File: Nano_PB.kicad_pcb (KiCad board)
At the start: 2 copper layers, 100 x 40 mm, 97 parts, among them CON1 BARREL_JACK, P1 CONN_01X06, P2 CONN_01X01, P3 CONN_01X03, P4 CONN_01X03, P5 CONN_01X03, P6 CONN_01X04, Q1 SMBT3904, Q10 BSS138, Q2 SMBT3904, Q3 SMBT3904, Q4 SMBT3904, Q5 SMBT3904, Q6 BC846B, Q7 BC846B, Q8 BC846B, Q9 BSS138, SW1 Izquierda, SW2 Arriba, SW3 Abajo, SW4 Derecha, U1 Arduino_Nano, U2 LM7805CT, U3 Matriz_5x7, U4 74HC595, U5 74HC595, U6 74HC148, U7 MMA7660FC

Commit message: corrige issue #10
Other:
- board text added: "ClkIn-D13"
- board text added: "Din-D12"
- board text removed: "ClkIn-D12"
- board text removed: "Din-D13"
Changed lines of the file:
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@@
-(kicad_pcb (version 4) (host pcbnew 4.1.0-alpha+201608060946+7009~46~ubuntu14.04.1-product)
+(kicad_pcb (version 20160815) (host pcbnew 4.1.0-alpha+201608271546+7097~46~ubuntu14.04.1-product)
   (general
     (links 193)
@@
     (uvia_dia 0.3)
     (uvia_drill 0.1)
+    (diff_pair_gap 0.25)
+    (diff_pair_width 0.2)
     (add_net +3V3)
     (add_net A0)
@@
     (uvia_dia 0.3)
     (uvia_drill 0.1)
+    (diff_pair_gap 0.25)
+    (diff_pair_width 0.2)
     (add_net +5V)
     (add_net "Net-(CON1-Pad1)")
@@
     (effects (font (size 1 1) (thickness 0.15)) (justify mirror))
   )
-  (gr_text ClkIn-D12 (at 84.26 70.24) (layer B.SilkS)
+  (gr_text ClkIn-D13 (at 84.26 70.24) (layer B.SilkS)
     (effects (font (size 1 1) (thickness 0.15)) (justify mirror))
   )
-  (gr_text Din-D13 (at 84.97 68.19) (layer B.SilkS)
+  (gr_text Din-D12 (at 84.97 68.19) (layer B.SilkS)
     (effects (font (size 1 1) (thickness 0.15)) (justify mirror))
   )

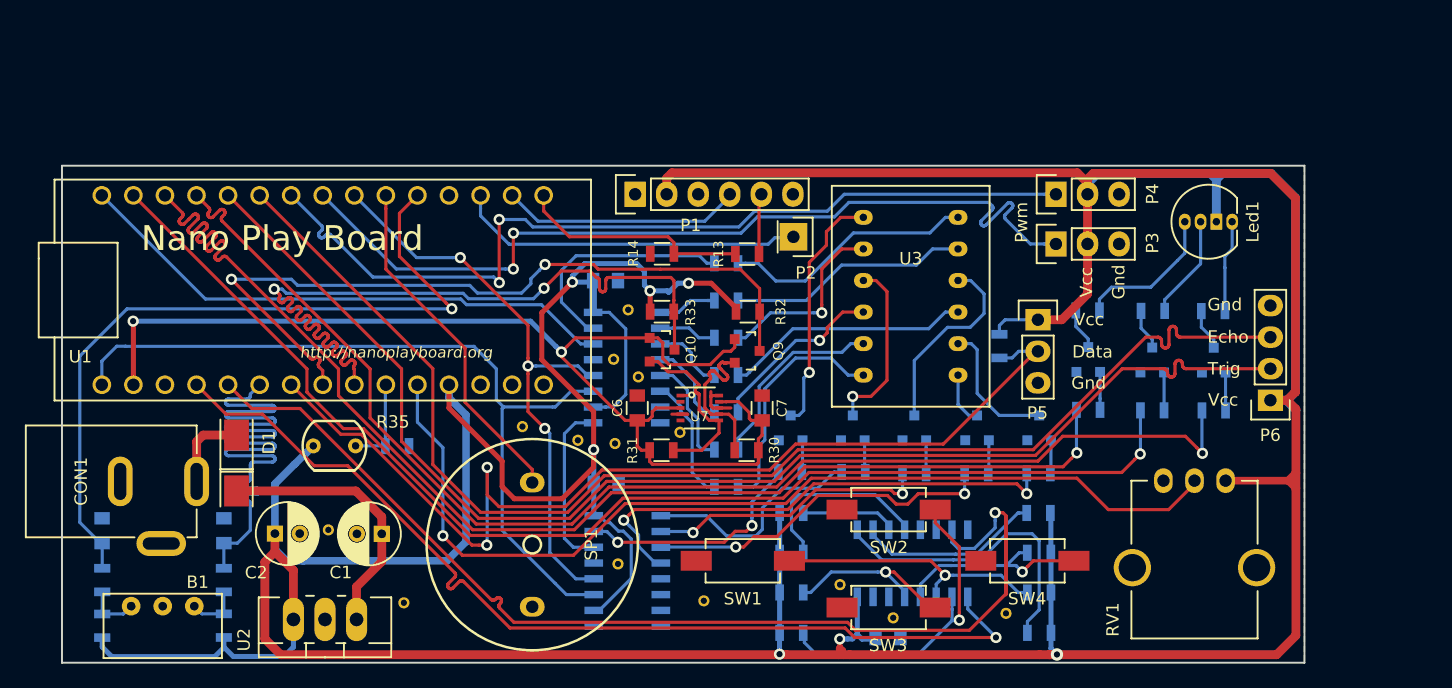
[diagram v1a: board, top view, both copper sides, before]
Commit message: cambiados encoder y potenciometro
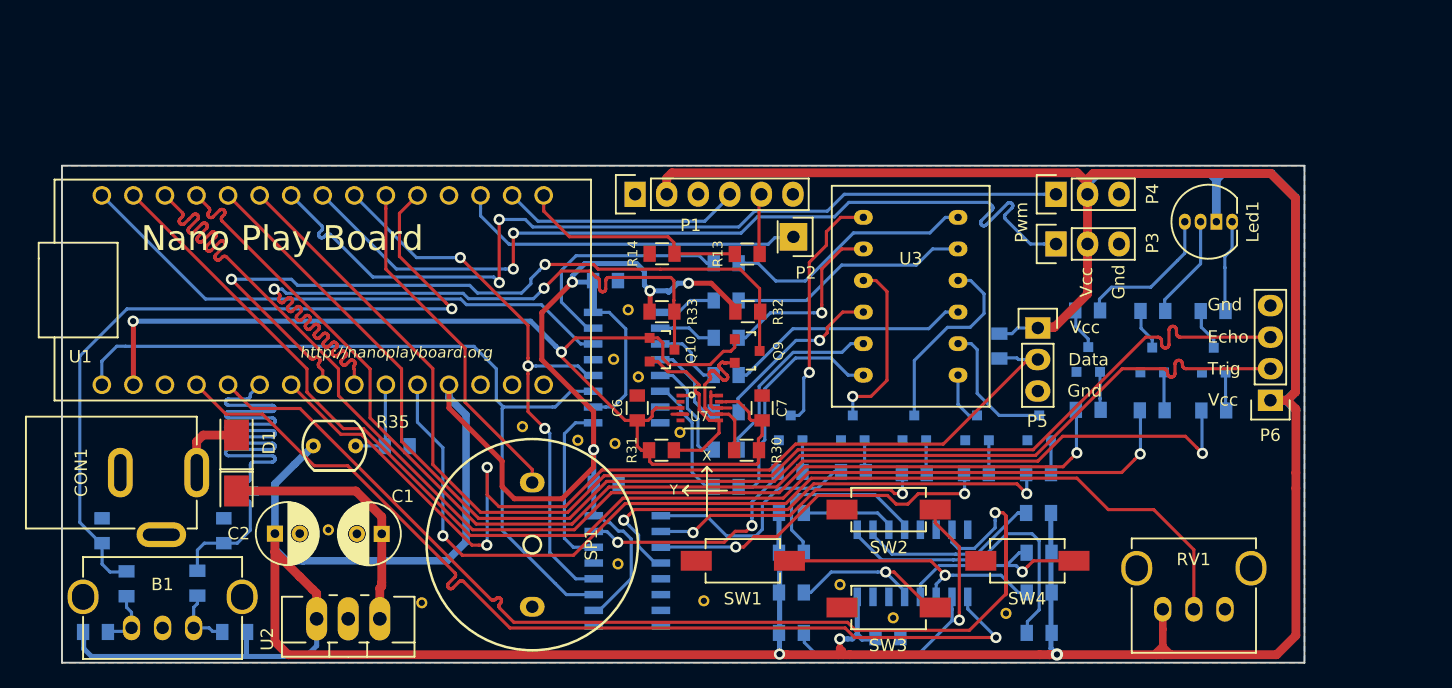
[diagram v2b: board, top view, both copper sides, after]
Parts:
- B1: footprint Sensores:Bourns_3315C_encoder_incremental -> Sensores:ALPS_EC12E24_encoder_incremental
- R1, R10, R11, R12, R13, R14, R15, R16, R17, R18, R19, R2, R20, R21, R22, R23, R24, R25, R26, R27, R28, R29, R3, R30, R31, R32, R33, R36, R37, R38, R39, R4, R40, R5, R6, R7, R8, R9: footprint Resistors_SMD:R_0805 -> Resistencias:R_0805
- RV1: footprint Potenciometros:POT_SR_PASIVES_R9011 -> Potenciometros:ALP_RK09K111
- moved RV1 10.4 mm to (143.2, 70.5), turned to 0 degrees
- moved R40 2.14 mm to (63.0, 68.4)
- moved R38 1.98 mm to (57.3, 68.4)
- moved U2 1.87 mm to (75.1, 71.2)
- moved B1 1.75 mm to (60.2, 72.0), turned to 0 degrees
- moved Gnd-Via 1.44 mm to (81.0, 70.0)
- moved R39 1.01 mm to (66.0, 72.3), turned to 180 degrees
- moved R37 0.74 mm to (54.8, 72.3), turned to 0 degrees
- moved CON1 0.71 mm to (62.9, 59.5)
- moved P5 0.66 mm to (130.6, 47.8)
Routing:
- net A7: track 78.9 -> 83.8 mm
- net +5V: track 477.2 -> 479.9 mm
- net A2: track 61.0 -> 63.1 mm
- net D2: track 60.9 -> 62.8 mm
- net Net-(C1-Pad1): track 21.6 -> 20.8 mm
- net Net-(B1-PadB): track 4.41 -> 5.19 mm
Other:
- board text added: "10/16"
- board text added: "Rev-0.2.1"
- board text added: "X"
- board text added: "Y"
- board text removed: "08/16"
- board text removed: "Rev-0.2"

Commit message: añadidos driver para led y conectores para fotodiodos infrarrojos
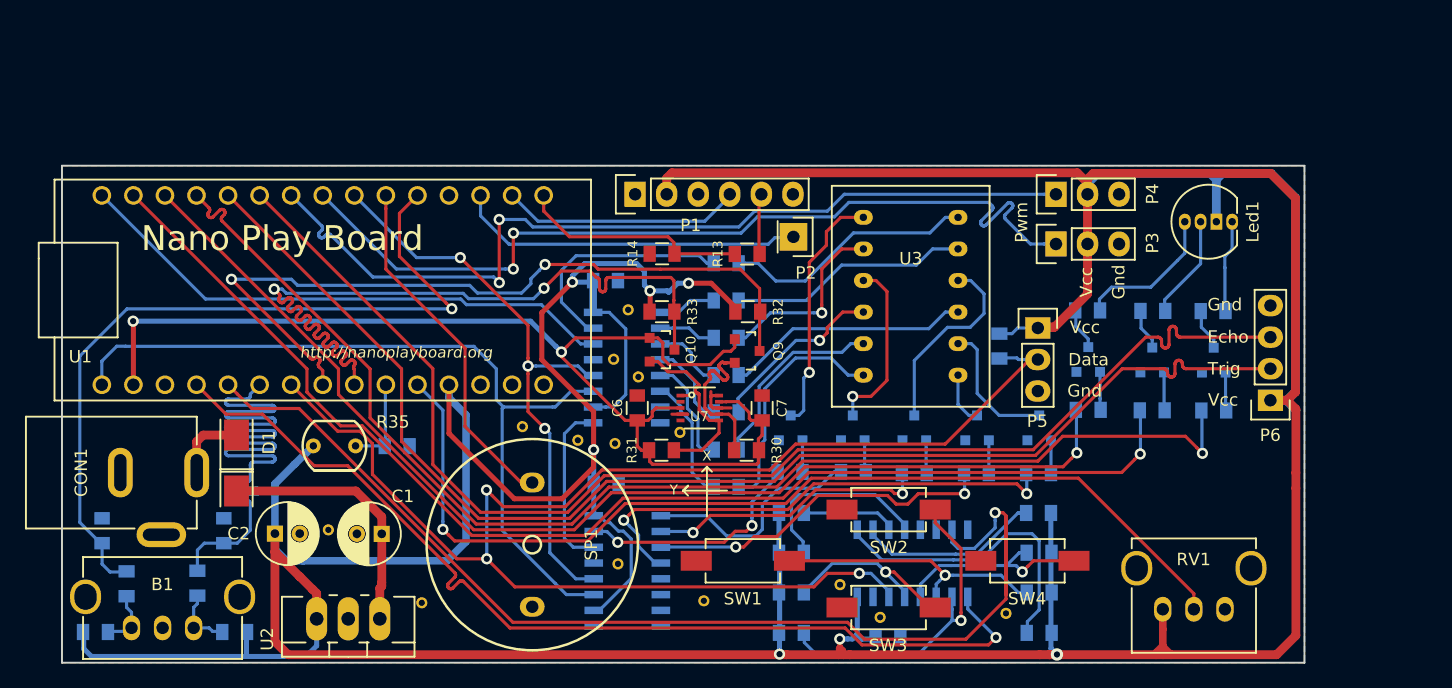
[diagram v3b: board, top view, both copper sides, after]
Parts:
- moved Gnd-Via 1.05 mm to (117.9, 71.1)
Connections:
- U6 pad 14: Net-(U6-Pad14) -> A3
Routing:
- net A3: track 82.6 -> 116.6 mm, vias 2 -> 3
- net D10: track 103.0 -> 91.8 mm
- net A7: track 83.8 -> 80.5 mm
- net Net-(R25-Pad2): track 15.1 -> 15.7 mm
- net D3: track 28.0 -> 28.5 mm

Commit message: finalizado enrutado provisional
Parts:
- removed G***: LOGO, logos:osh-logo
- removed G***: LOGO, logos:logo_HackLabAl
- removed the Gnd-Via at (101.8, 56.2)
- removed the Gnd-Via at (93.6, 56.9)
- removed the Gnd-Via at (103.8, 69.8)
- removed the Gnd-Via at (114.7, 68.5)
- removed the Gnd-Via at (96.5, 50.4)
- removed the Gnd-Via at (128.1, 70.8)
- removed the Gnd-Via at (81.0, 70.0)
- removed the Gnd-Via at (117.9, 71.1)
- removed the Gnd-Via at (97.7, 46.4)
- removed the Gnd-Via at (98.5, 51.8)
- removed the Gnd-Via at (73.5, 64.1)
- removed the Gnd-Via at (96.6, 57.1)
- removed the Gnd-Via at (96.8, 66.8)
- removed the Gnd-Via at (89.2, 55.8)
- removed the P3 at (132.1, 41.1)
- removed the Q6 at (144.8, 50.4)
- removed the Q7 at (134.7, 50.4)
- removed Q8: BC846B, TO_SOT_Packages_SMD:SOT-23
- added C10: 1u, Capacitors_SMD:C_0805, F.Cu at (139.3, 34.0)
- added C11: 1u, Capacitors_SMD:C_0805, F.Cu at (139.3, 37.3)
- added C17: 100n, Capacitors_SMD:C_0805, F.Cu at (145.2, 38.1)
- added C18: 10n, Capacitors_SMD:C_0805, B.Cu at (144.5, 43.5)
- added C19: 100n, Capacitors_SMD:C_0805, F.Cu at (145.1, 61.8)
- added C20: 10n, Capacitors_SMD:C_0805, B.Cu at (142.3, 63.4)
- added C21: 100n, Capacitors_SMD:C_0805, B.Cu at (140.7, 55.9)
- added C5: 10u, Capacitors_Tantalum_SMD:Tantalum_Case-A_EIA-3216-18_Reflow, F.Cu at (97.5, 30.6)
- added C7: 100n, Capacitors_SMD:C_0805, B.Cu at (112.0, 59.2)
- added C8: 1u, Capacitors_SMD:C_0805, F.Cu at (139.3, 27.6)
- added C9: 1u, Capacitors_SMD:C_0805, F.Cu at (139.3, 31.0)
- added Gnd-Via: VAL**, Vias:Gnd-Via, F.Cu at (54.6, 31.6)
- added Gnd-Via: VAL**, Vias:Gnd-Via, F.Cu at (54.7, 72.2)
- added Gnd-Via: VAL**, Vias:Gnd-Via, F.Cu at (149.5, 72.2)
- added Gnd-Via: VAL**, Vias:Gnd-Via, F.Cu at (117.4, 72.4)
- added Gnd-Via: VAL**, Vias:Gnd-Via, F.Cu at (88.0, 68.8)
- added Gnd-Via: VAL**, Vias:Gnd-Via, F.Cu at (91.2, 67.2)
- added Gnd-Via: VAL**, Vias:Gnd-Via, F.Cu at (107.1, 56.3)
- added Gnd-Via: VAL**, Vias:Gnd-Via, F.Cu at (103.2, 55.9)
- added Gnd-Via: VAL**, Vias:Gnd-Via, F.Cu at (137.0, 26.7)
- added Gnd-Via: VAL**, Vias:Gnd-Via, F.Cu at (137.0, 29.9)
- added Gnd-Via: VAL**, Vias:Gnd-Via, F.Cu at (137.0, 33.1)
- added Gnd-Via: VAL**, Vias:Gnd-Via, F.Cu at (85.3, 48.4)
- added Gnd-Via: VAL**, Vias:Gnd-Via, F.Cu at (137.0, 36.3)
- added Gnd-Via: VAL**, Vias:Gnd-Via, F.Cu at (106.2, 52.1)
- added Gnd-Via: VAL**, Vias:Gnd-Via, F.Cu at (102.6, 56.8)
- added Gnd-Via: VAL**, Vias:Gnd-Via, F.Cu at (92.5, 50.6)
- added Gnd-Via: VAL**, Vias:Gnd-Via, F.Cu at (94.3, 45.0)
- added Gnd-Via: VAL**, Vias:Gnd-Via, F.Cu at (93.2, 45.0)
- added Gnd-Via: VAL**, Vias:Gnd-Via, F.Cu at (117.8, 56.3)
- added Gnd-Via: VAL**, Vias:Gnd-Via, F.Cu at (140.4, 25.4)
- added Gnd-Via: VAL**, Vias:Gnd-Via, F.Cu at (149.6, 27.2)
- added P1: CONN_02X04, Socket_Strips:Socket_Strip_Straight_2x04, F.Cu at (101.1, 29.6)
- added P11: CONN_01X04, Pin_Headers:Pin_Header_Angled_1x04_Pitch2.54mm, F.Cu at (148.1, 34.0)
- added P12: CONN_01X04, Pin_Headers:Pin_Header_Angled_1x04_Pitch2.54mm, F.Cu at (148.1, 57.7)
- added P5: CONN_01X03, Pin_Headers:Pin_Header_Straight_1x03_Pitch2.54mm, F.Cu at (130.5, 30.9)
- added P6: CONN_01X03, Pin_Headers:Pin_Header_Straight_1x03_Pitch2.54mm, F.Cu at (130.5, 34.1)
- added P7: CONN_01X03, Pin_Headers:Pin_Header_Straight_1x03_Pitch2.54mm, F.Cu at (130.5, 37.3)
- added P9: CONN_01X04, Socket_Strips:Socket_Strip_Straight_1x04, F.Cu at (134.1, 45.2)
- added R21: 120, Resistencias:R_0805, B.Cu at (142.0, 33.0)
- added R22: 120, Resistencias:R_0805, B.Cu at (143.9, 33.0)
- added R36: 10K, Resistencias:R_0805, B.Cu at (83.1, 49.0)
- added R43: 220R, Resistencias:R_0805, B.Cu at (144.6, 36.6)
- added R44: 47K, Resistencias:R_0805, B.Cu at (144.5, 41.6)
- added R45: 220R, Resistencias:R_0805, B.Cu at (144.2, 60.3)
- added R46: 47K, Resistencias:R_0805, B.Cu at (145.3, 63.4)
- added U6: PCA9551, Housings_SSOP:TSSOP-16_4.4x5mm_Pitch0.65mm, B.Cu at (116.8, 57.3)
- added U9: 40106, Housings_SOIC:SOIC-16_3.9x9.9mm_Pitch1.27mm, B.Cu at (140.7, 49.5)
- D1: moved to B.Cu
- P4: footprint Pin_Headers:Pin_Header_Straight_1x03 -> Pin_Headers:Pin_Header_Straight_1x03_Pitch2.54mm
- R15, R16, R17: value 4K7 -> 10K
- R18, R19: value 100 -> 10K
- R20: value 100 -> 120
- moved R16 27.7 mm to (127.5, 27.7), turned to 0 degrees
- moved R17 26.6 mm to (127.5, 30.9), turned to 0 degrees
- moved R18 21.2 mm to (127.5, 34.1), turned to 0 degrees
- moved C15 20.1 mm to (75.3, 66.0), turned to 270 degrees
- moved R15 19.6 mm to (125.9, 59.7)
- moved R42 18.5 mm to (81.3, 66.0)
- moved R37 17.2 mm to (91.2, 58.4)
- moved R41 16.7 mm to (82.7, 72.6)
- moved B1 16.5 mm to (76.7, 72.2)
- moved R39 15.9 mm to (70.7, 72.6)
- moved SP1 15.9 mm to (78.0, 54.8)
- moved SW1 15.6 mm to (91.3, 67.0)
- moved R40 15.2 mm to (72.3, 66.0)
- moved R20 14.7 mm to (145.8, 33.0), turned to 270 degrees
- moved C16 12.9 mm to (77.9, 66.0), turned to 270 degrees
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- renumbered C5 to C12, C6 to C13, C7 to C14, C8 to C15, C9 to C16, P6 to P10, P1 to P2, P2 to P3, P5 to P8, Q9 to Q6, Q10 to Q7, R21 to R23, R22 to R24, R26 to R25, R23 to R26, R24 to R28, R28 to R29, R25 to R30, R29 to R31, R30 to R32, R31 to R33, R32 to R34, R33 to R35, R35 to R37, R36 to R38, R37 to R39, R38 to R40, R39 to R41, R40 to R42, U4 to U3, U5 to U4, U3 to U5, U6 to U7, U7 to U8
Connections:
- C16 pad 1: A2 -> D5
- P2 pad 4: D0 -> D10
- P2 pad 5: Net-(P1-Pad5) -> /Bluetooth/RxD
- P4 pad 1: D6 -> SERVO1
- P8 pad 1: +5V -> A3
- P8 pad 2: A3 -> +5V
- R13 pad 1: Net-(P1-Pad5) -> /Bluetooth/RxD
- R13 pad 2: D1 -> D11
- R14 pad 1: D1 -> /Bluetooth/RxD
- R15 pad 1: Net-(Q6-Pad1) -> +5V
- R15 pad 2: D9 -> Net-(R15-Pad2)
- R16 pad 1: Net-(Q7-Pad1) -> +5V
- R16 pad 2: D10 -> SERVO1
- R17 pad 1: Net-(Q8-Pad1) -> +5V
- R17 pad 2: D11 -> SERVO2
- R18 pad 1: Net-(Led1-Pad4) -> +5V
- R18 pad 2: Net-(Q6-Pad3) -> SERVO3
- R19 pad 1: Net-(Led1-Pad1) -> +5V
- R19 pad 2: Net-(Q7-Pad3) -> SERVO4
- R20 pad 1: Net-(Led1-Pad2) -> Net-(Led1-Pad4)
- R20 pad 2: Net-(Q8-Pad3) -> LED_RED
- R42 pad 2: A2 -> D5
- SP1 pad 1: D3 -> BUZZER
- U1 pad 1: D1 -> Net-(U1-Pad1)
- U1 pad 2: D0 -> Net-(U1-Pad2)
- U7 pad 14: A3 -> A2
- U8 pad 5: Net-(U7-Pad5) -> D3
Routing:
- net +5V: track 479.9 -> 669.6 mm, vias 7 -> 5
- net +3V3: track 91.5 -> 184.2 mm, vias 2 -> 4
- net BUZZER: track 0.00 -> 52.0 mm, vias 0 -> 1
- net D11: track 99.7 -> 55.4 mm, vias 1 -> 2
- net A3: track 116.6 -> 72.4 mm, vias 3 -> 2
- net LED_RED: track 0.00 -> 43.2 mm
- net LED_BLUE: track 0.00 -> 42.0 mm
- net LED_GREEN: track 0.00 -> 41.3 mm
- net SERVO1: track 0.00 -> 38.6 mm, vias 0 -> 1
- net SERVO2: track 0.00 -> 36.0 mm, vias 0 -> 1
- net SERVO3: track 0.00 -> 32.6 mm, vias 0 -> 1
- net SERVO4: track 0.00 -> 28.4 mm
- net D3: track 28.5 -> 56.5 mm, vias 0 -> 2
- net D5: track 72.0 -> 44.4 mm, vias 2 -> 0
- net D10: track 91.8 -> 68.1 mm, vias 1 -> 2
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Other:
- board size 100 x 40 mm -> 100 x 50 mm
- net class Default: via_dia 0.9 -> 0.8; via_drill 0.5 -> 0.4
- net class Power: via_dia 1 -> 0.8; via_drill 0.5 -> 0.4

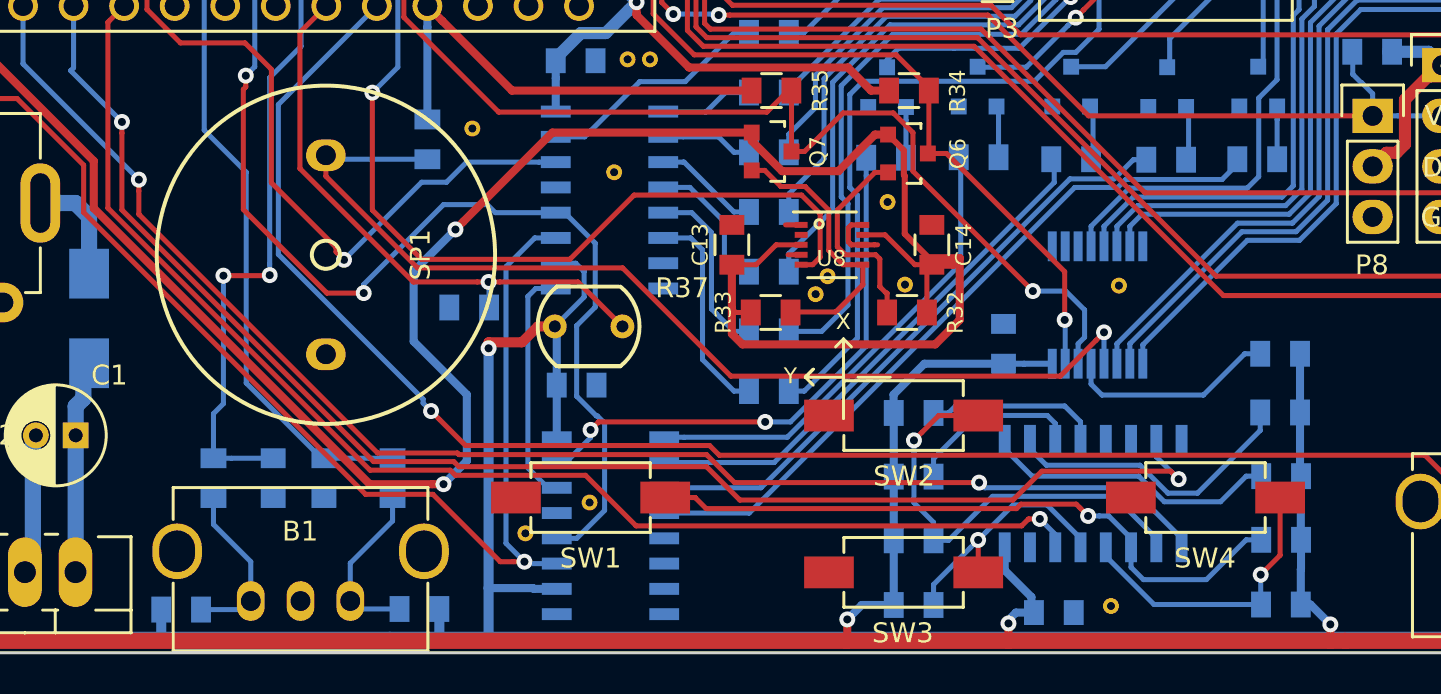
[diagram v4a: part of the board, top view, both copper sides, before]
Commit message: Modificada posicion pulsadores y añadir vias entre planos de masa
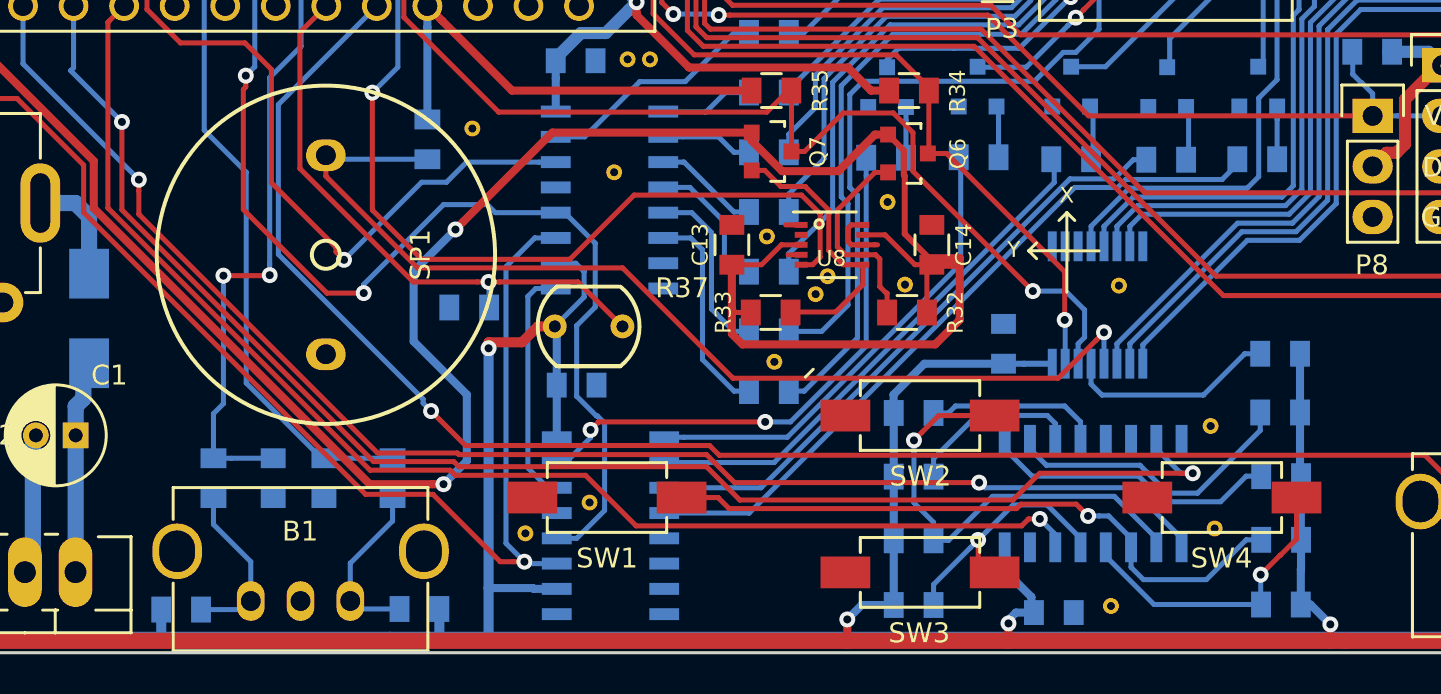
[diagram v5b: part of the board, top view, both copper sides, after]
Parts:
- added Gnd-Via: VAL**, Vias:Gnd-Via, F.Cu at (100.5, 60.1)
- added Gnd-Via: VAL**, Vias:Gnd-Via, F.Cu at (100.2, 53.9)
- added Gnd-Via: VAL**, Vias:Gnd-Via, F.Cu at (122.7, 68.5)
- added Gnd-Via: VAL**, Vias:Gnd-Via, F.Cu at (122.5, 63.4)
- moved SW2 0.83 mm to (107.8, 62.9)
- moved SW3 0.83 mm to (107.8, 70.7)
- moved SW4 0.83 mm to (123.0, 67.0)
- moved SW1 0.82 mm to (92.1, 67.0)
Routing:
- net Net-(R26-Pad2): track 33.5 -> 35.4 mm
- net A1: track 73.7 -> 74.6 mm
